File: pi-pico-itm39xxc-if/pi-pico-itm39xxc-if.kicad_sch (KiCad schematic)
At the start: 1 part

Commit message: Working on pico itm interface
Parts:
- added C?: DNP, Capacitor_SMD:C_0805_2012Metric, symbol Device:C_Small
- added D? (x3): LED_Small_Filled, LED_SMD:LED_0805_2012Metric_Pad1.15x1.40mm_HandSolder, symbol Device:LED_Small_Filled
- added D?: BAT60, Diode_SMD:D_SOD-323_HandSoldering, symbol Device:D_Schottky_Small_Filled
- added J? (x3): Conn_01x03, Connector_PinHeader_2.54mm:PinHeader_1x03_P2.54mm_Vertical, symbol Connector_Generic:Conn_01x03
- added J?: Conn_01x10, TerminalBlock_Phoenix:TerminalBlock_Phoenix_MKDS-3-10-5.08_1x10_P5.08mm_Horizontal, symbol Connector_Generic:Conn_01x10
- added R? (x2): 1k, Resistor_SMD:R_0805_2012Metric, symbol Device:R_Small
- added R?: 47R, Resistor_SMD:R_0805_2012Metric, symbol Device:R_Small
- added R?: DNP, Resistor_SMD:R_0805_2012Metric, symbol Device:R_Small
- added R?: 2k, Resistor_SMD:R_0805_2012Metric, symbol Device:R_Small
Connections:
- net DAC_A1: now also J?.8 (Pin_8)
- net DAC_A2: now also J?.9 (Pin_9)
- net DAC_A3: now also J?.10 (Pin_10)
- net DAC_REF: now also R?.1
- net GND: now also C?.2, J?.3 (Pin_3), J?.3 (Pin_3), J?.3 (Pin_3), J?.3 (Pin_3), J?.4 (Pin_4), R?.2, R?.2, R?.2
- net PICO_GPIO4: now also J?.2 (Pin_2)
- net PICO_GPIO5: now also J?.1 (Pin_1)
- net RS232_RX2: now also J?.1 (Pin_1)
- net RS232_RX2_TTL: now also J?.1 (Pin_1)
- net RS232_TX2: now also J?.2 (Pin_2)
- net RS232_TX2_TTL: now also J?.2 (Pin_2)
- net PICO_GPIO0: now reaches U?.1 (GPIO0)
- net PICO_GPIO0: now also J?.1 (Pin_1)
- net LED_2: now reaches U?.10 (GPIO7)
- net LED_2: now also D?.2 (A)
- net PICO_GPIO9: now reaches U?.12 (GPIO9)
- net PICO_GPIO1: now reaches U?.2 (GPIO1)
- net PICO_GPIO1: now also J?.2 (Pin_2)
- net PICO_GPIO22: now reaches U?.29 (GPIO22)
- net PICO_GPIO28: now reaches U?.34 (GPIO28_ADC2)
- net ADC_VREF: now reaches U?.35 (ADC_VREF)
- net ADC_VREF: now also C?.1, R?.2, R?.2
- net +3V3: now reaches U?.36 (3V3)
- net +3V3: now also R?.1
- net at U?.39 (VSYS): now also D?.1 (K)
- net PICO_GPIO2: now reaches U?.4 (GPIO2)
- net PICO_GPIO3: now reaches U?.5 (GPIO3)
- net LED_1: now reaches U?.9 (GPIO6)
- net LED_1: now also D?.2 (A)
- new net: D?.1 (K), R?.1 (x3)
- new net +5V: D?.2 (A), D?.2 (A)
- new net Im: J?.6 (Pin_6)
- new net Vm: J?.5 (Pin_5)
- no-connect marks 0 -> 7
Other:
- sheet tps56320x_3v3 renamed tps56320x_5v
- sheet tps56320x_5v: file tps56320x_3v3.kicad_sch -> tps56320x_5v.kicad_sch
- sheet tps56320x_5v ports: added 5V; removed 3V3
- sheet ttl_rs232_max3232 ports: added Vdd; removed Vcc
- note added: "Additional RS232"
- note added: "Expanded UART0"
- note added: "LEDs"
- note added: "UART0"
- note added: "[1]"
- note added: "[2]"
- note added: "[3]"
- note removed: "ADD LEDS?"

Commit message: Finishing schematics of pico itm if
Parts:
- added H? (x7): MountingHole, MountingHole:MountingHole_3.2mm_M3, symbol Mechanical:MountingHole
- added J? (x4): Conn_01x02, TerminalBlock_Phoenix:TerminalBlock_Phoenix_MKDS-1,5-2-5.08_1x02_P5.08mm_Horizontal, symbol Connector_Generic:Conn_01x02
- added J?: Conn_02x05_Counter_Clockwise, symbol Connector_Generic:Conn_02x05_Counter_Clockwise
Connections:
- net +12V: now also J?.1 (Pin_1), J?.1 (Pin_1)
- net +3V3: now also J?.1 (Pin_1)
- net +5V: now also J?.1 (Pin_1), J?.1 (Pin_1)
- net GND: now also J?.2 (Pin_2), J?.2 (Pin_2), J?.2 (Pin_2), J?.2 (Pin_2), J?.2 (Pin_2)
- net PICO_GPIO16: now also J?.9 (Pin_9)
- net PICO_GPIO17: now also J?.7 (Pin_7)
- net PICO_GPIO18: now also J?.6 (Pin_6)
- net PICO_GPIO19: now also J?.8 (Pin_8)
- net PICO_GPIO20: now also J?.3 (Pin_3)
- net PICO_GPIO21: now also J?.4 (Pin_4)
- no-connect marks 7 -> 9
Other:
- note added: "Additional LEDs"
- note added: "External W5500"
- note added: "External W5500 mounting holes"
- note added: "IT-E167 connector"
- note added: "Input voltages [2]"
- note added: "Measurements conditioning"
- note added: "Mounting holes"
- note added: "Output voltages [3]"
- note added: "Pico/Pico-EVB"
- note added: "RS232 driver/receiver"
- note added: "Supply"
- note added: "Supply - 12V/6W The design should work with the regular Pico board or with the W5500-EVB-Pico board. Design notes [1] In this design, the DAC module generates a 3 V reference signal. This signal is used as the reference for the signal conditioning module, in order to place the -10 V ~ 10 V analog signal to the 0 ~ 3 V range. That's why the DAC_REF signal is fed to the signal conditioning circuit.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"
- note added: "[4]"
- note added: "[5]"
- note removed: "[2]"
- note removed: "[3]"
- moved on the sheet: C?, D?, J?, R?, U?

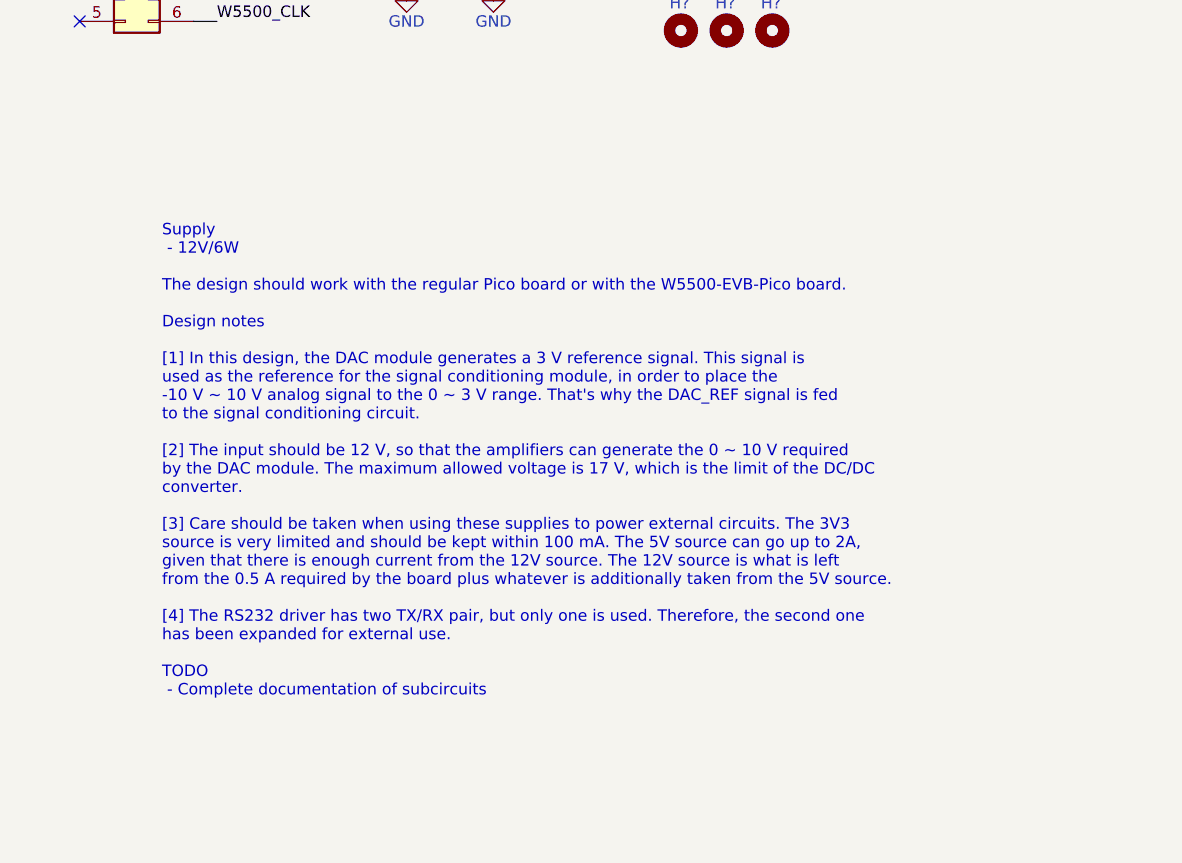
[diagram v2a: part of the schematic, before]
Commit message: Added docs for subcircuits
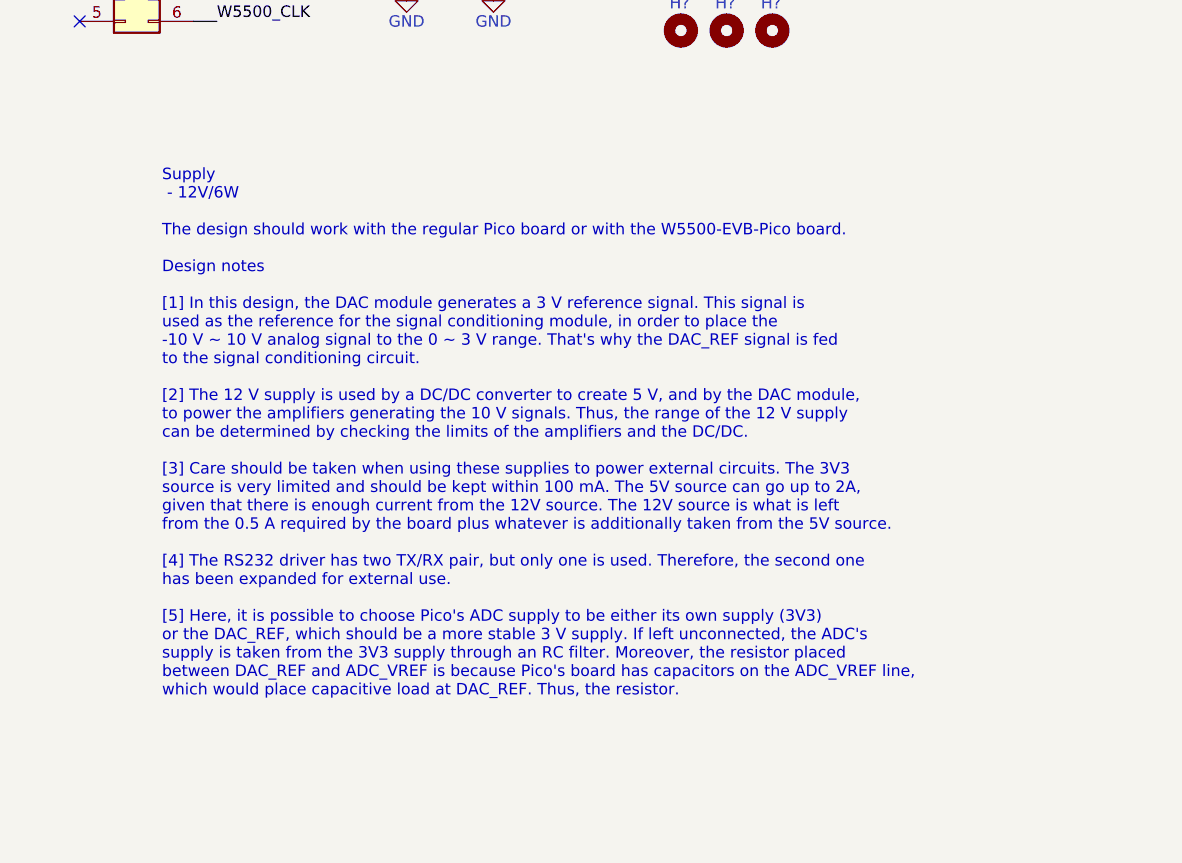
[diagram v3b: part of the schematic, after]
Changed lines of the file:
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@@
     (effects (font (size 1.27 1.27)) (justify left bottom))
   )
-  (text "Supply\n - 12V/6W\n\nThe design should work with the regular Pico board or with the W5500-EVB-Pico board.\n\nDesign notes\n\n[1] In this design, the DAC module generates a 3 V reference signal. This signal is\nused as the reference for the signal conditioning module, in order to place the \n-10 V ~ 10 V analog signal to the 0 ~ 3 V range. That's why the DAC_REF signal is fed\nto the signal conditioning circuit.\n\n[2] The input should be 12 V, so that the amplifiers can generate the 0 ~ 10 V required\nby the DAC module. The maximum allowed voltage is 17 V, which is the limit of the DC/DC\nconverter.\n\n[3] Care should be taken when using these supplies to power external circuits. The 3V3 \nsource is very limited and should be kept within 100 mA. The 5V source can go up to 2A,\ngiven that there is enough current from the 12V source. The 12V source is what is left\nfrom the 0.5 A required by the board plus whatever is additionally taken from the 5V source.\n\n[4] The RS232 driver has two TX/RX pair, but only one is used. Therefore, the second one\nhas been expanded for external use.\n\nTODO\n - Complete documentation of subcircuits"
+  (text "Supply\n - 12V/6W\n\nThe design should work with the regular Pico board or with the W5500-EVB-Pico board.\n\nDesign notes\n\n[1] In this design, the DAC module generates a 3 V reference signal. This signal is\nused as the reference for the signal conditioning module, in order to place the \n-10 V ~ 10 V analog signal to the 0 ~ 3 V range. That's why the DAC_REF signal is fed\nto the signal conditioning circuit.\n\n[2] The 12 V supply is used by a DC/DC converter to create 5 V, and by the DAC module,\nto power the amplifiers generating the 10 V signals. Thus, the range of the 12 V supply\ncan be determined by checking the limits of the amplifiers and the DC/DC.\n\n[3] Care should be taken when using these supplies to power external circuits. The 3V3 \nsource is very limited and should be kept within 100 mA. The 5V source can go up to 2A,\ngiven that there is enough current from the 12V source. The 12V source is what is left\nfrom the 0.5 A required by the board plus whatever is additionally taken from the 5V source.\n\n[4] The RS232 driver has two TX/RX pair, but only one is used. Therefore, the second one\nhas been expanded for external use.\n\n[5] Here, it is possible to choose Pico's ADC supply to be either its own supply (3V3)\nor the DAC_REF, which should be a more stable 3 V supply. If left unconnected, the ADC's\nsupply is taken from the 3V3 supply through an RC filter. Moreover, the resistor placed \nbetween DAC_REF and ADC_VREF is because Pico's board has capacitors on the ADC_VREF line,\nwhich would place capacitive load at DAC_REF. Thus, the resistor."
     (at 185.928 149.352 0)
     (effects (font (size 1.27 1.27)) (justify left bottom))

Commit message: Passing ERC
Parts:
- C1: renamed from C?; footprint Capacitor_SMD:C_0805_2012Metric -> Capacitor_SMD:C_0805_2012Metric_Pad1.18x1.45mm_HandSolder
- J5: renamed from J?; footprint (none) -> Connector_PinHeader_2.54mm:PinHeader_2x05_P2.54mm_Vertical
- R1, R2, R3, R4, R5: renamed from R?; footprint Resistor_SMD:R_0805_2012Metric -> Resistor_SMD:R_0805_2012Metric_Pad1.20x1.40mm_HandSolder
- gave numbers to parts that had none: 20
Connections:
- net PICO_GPIO4: no longer J6.2 (Pin_2)
- net PICO_GPIO5: no longer J6.1 (Pin_1)
- net RS232_RX1: now also J6.1 (Pin_1)
- net RS232_TX1: now also J6.2 (Pin_2)
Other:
- note added: "Power flags"
- moved on the sheet: D2, D3, H1, H2, H3, H4, H5, H6, H7, J1, J2, J3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

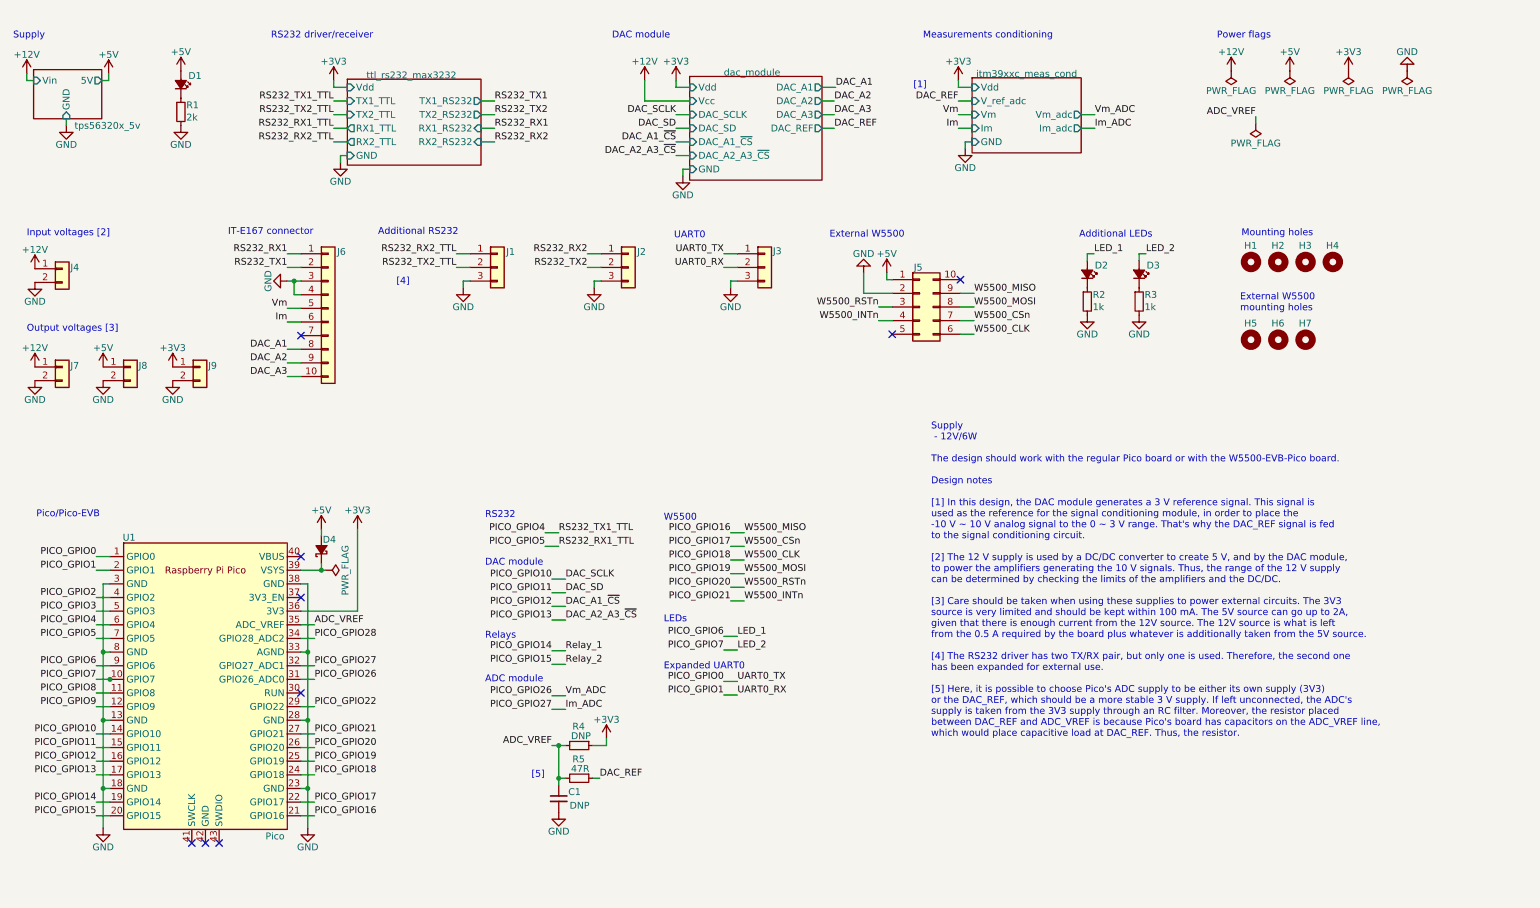
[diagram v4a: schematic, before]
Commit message: Expanded unused pico pins
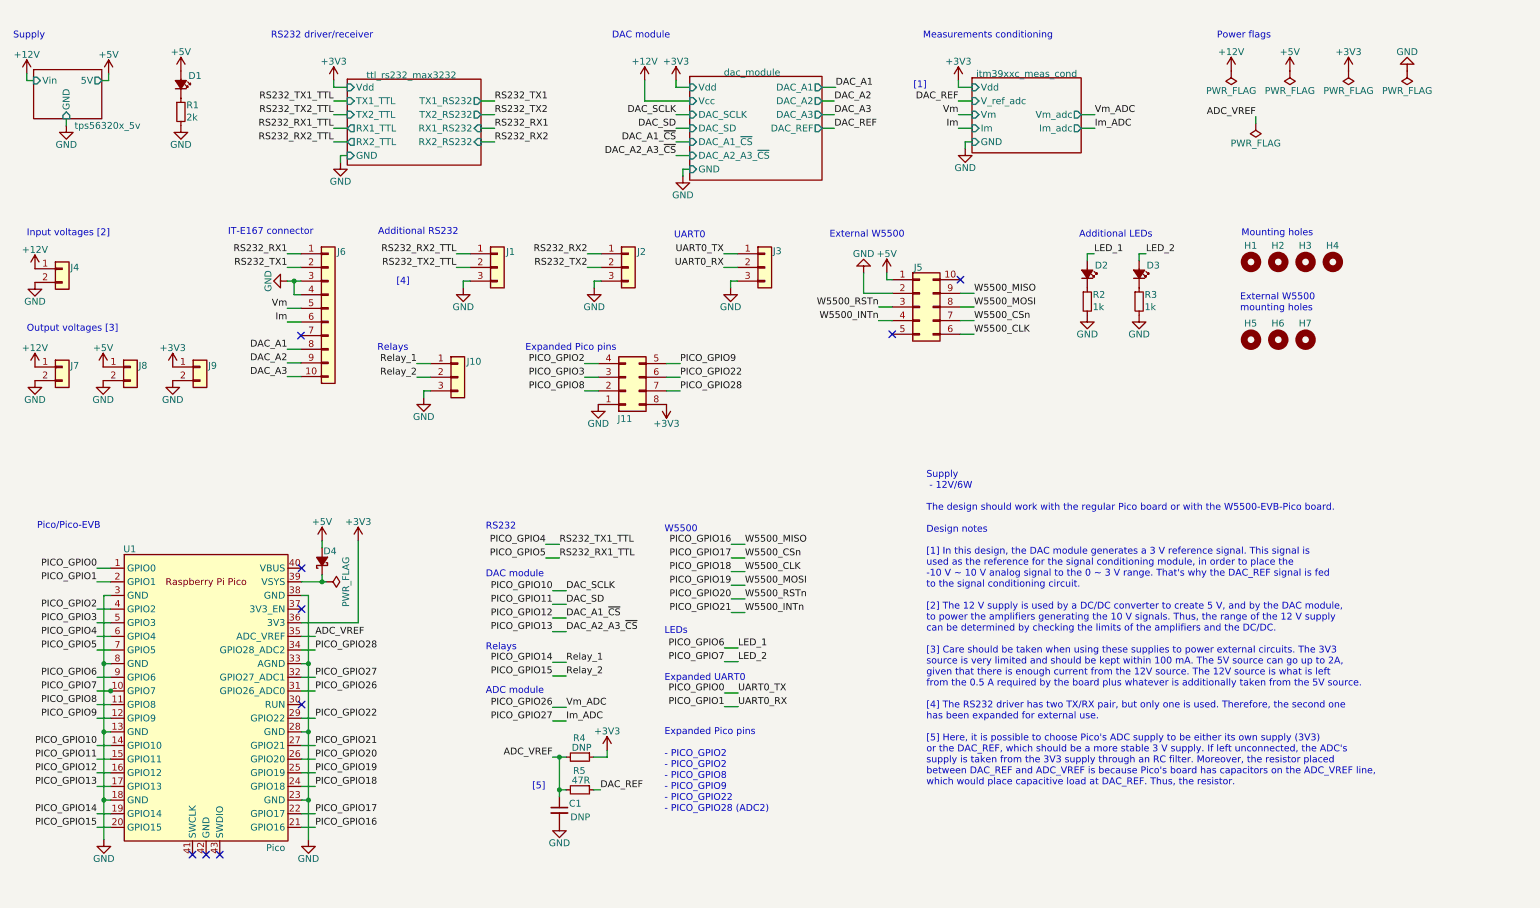
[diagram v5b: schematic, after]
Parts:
- added J10: Conn_01x03, Connector_PinHeader_2.54mm:PinHeader_1x03_P2.54mm_Vertical, symbol Connector_Generic:Conn_01x03
- added J11: Conn_02x04_Counter_Clockwise, Connector_PinHeader_2.54mm:PinHeader_2x04_P2.54mm_Vertical, symbol Connector_Generic:Conn_02x04_Counter_Clockwise
- J2: footprint Connector_PinHeader_2.54mm:PinHeader_1x03_P2.54mm_Vertical -> TerminalBlock_Phoenix:TerminalBlock_Phoenix_MKDS-1,5-3-5.08_1x03_P5.08mm_Horizontal
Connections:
- net +3V3: now also J11.8 (Pin_8)
- net GND: now also J10.3 (Pin_3), J11.1 (Pin_1)
- net PICO_GPIO14: now also J10.1 (Pin_1)
- net PICO_GPIO15: now also J10.2 (Pin_2)
- net PICO_GPIO2: now also J11.4 (Pin_4)
- net PICO_GPIO22: now also J11.6 (Pin_6)
- net PICO_GPIO28: now also J11.7 (Pin_7)
- net PICO_GPIO3: now also J11.3 (Pin_3)
- net PICO_GPIO8: now also J11.2 (Pin_2)
- net PICO_GPIO9: now also J11.5 (Pin_5)
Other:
- note added: "Expanded Pico pins"
- note added: "Expanded Pico pins - PICO_GPIO2 - PICO_GPIO2 - PICO_GPIO8 - PICO_GPIO9 - PICO_GPIO22 - PICO_GPIO28 (ADC2)"
- moved on the sheet: C1, D4, R4, R5, U1

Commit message: Fixed Pico and DAC footprints
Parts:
- U1: footprint RPi_Pico:RPi_Pico_SMD_TH -> CL_MCU_RaspberryPi_and_Boards:RPi_Pico_SMD_TH
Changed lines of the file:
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@@
     (property "Reference" "U1" (id 0) (at 36.703 114.173 0))
     (property "Value" "Pico" (id 1) (at 63.881 169.799 0))
-    (property "Footprint" "RPi_Pico:RPi_Pico_SMD_TH" (id 2) (at 50.927 141.859 90)
+    (property "Footprint" "CL_MCU_RaspberryPi_and_Boards:RPi_Pico_SMD_TH" (id 2) (at 50.927 141.859 90)
       (effects (font (size 1.27 1.27)) hide)
     )
@@
     )
     (path "/e537a71c-a3ba-4b5b-8bab-8ecb166d6a48"
-      (reference "U1") (unit 1) (value "Pico") (footprint "RPi_Pico:RPi_Pico_SMD_TH")
+      (reference "U1") (unit 1) (value "Pico") (footprint "CL_MCU_RaspberryPi_and_Boards:RPi_Pico_SMD_TH")
     )
     (path "/eac3a80a-bdd4-4793-93a3-28d6b9f0c36d/b70f6820-5f16-43a7-af28-07d093030925"
@@
     )
     (path "/2721c640-6df0-48bb-bbcb-b59a3c9df97e/8dabc0ef-c49f-460d-ba6c-c984c46040c1"
-      (reference "U7") (unit 1) (value "MCP4922") (footprint "Package_SO:SOIC-16_3.9x9.9mm_P1.27mm")
+      (reference "U7") (unit 1) (value "MCP4922") (footprint "Package_SO:SOIC-14_3.9x8.7mm_P1.27mm")
     )
     (path "/2721c640-6df0-48bb-bbcb-b59a3c9df97e/1e1d021d-0851-4b61-a3ac-ac46840f4527"
@@
     )
     (path "/2721c640-6df0-48bb-bbcb-b59a3c9df97e/e8e90e4d-712c-4c30-8b3c-313caa89c7ed"
-      (reference "U9") (unit 1) (value "MCP4922") (footprint "Package_SO:SOIC-16_3.9x9.9mm_P1.27mm")
+      (reference "U9") (unit 1) (value "MCP4922") (footprint "Package_SO:SOIC-14_3.9x8.7mm_P1.27mm")
     )
     (path "/692a73d2-e176-477f-bd1d-3a1a47774593/f08ee633-5528-498d-a37b-98234454325c"
